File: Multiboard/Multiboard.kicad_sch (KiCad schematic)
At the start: 51 parts, among them J1 Conn_01x20_Socket, J2 Conn_01x20_Socket, J3 Debug, J4 USB_C_Receptacle_USB2.0_16P, SW1 BOOT0, SW2 NRST, SW8 KEY, U1 STM32F411RET6, U3 USART1, U4 I2C1, U5 SPI1, U6 ADC, U7 GPIO-PWM, U8 MCP1792x-3302xCB, Y1 32.768KHz, Y2 25MHz

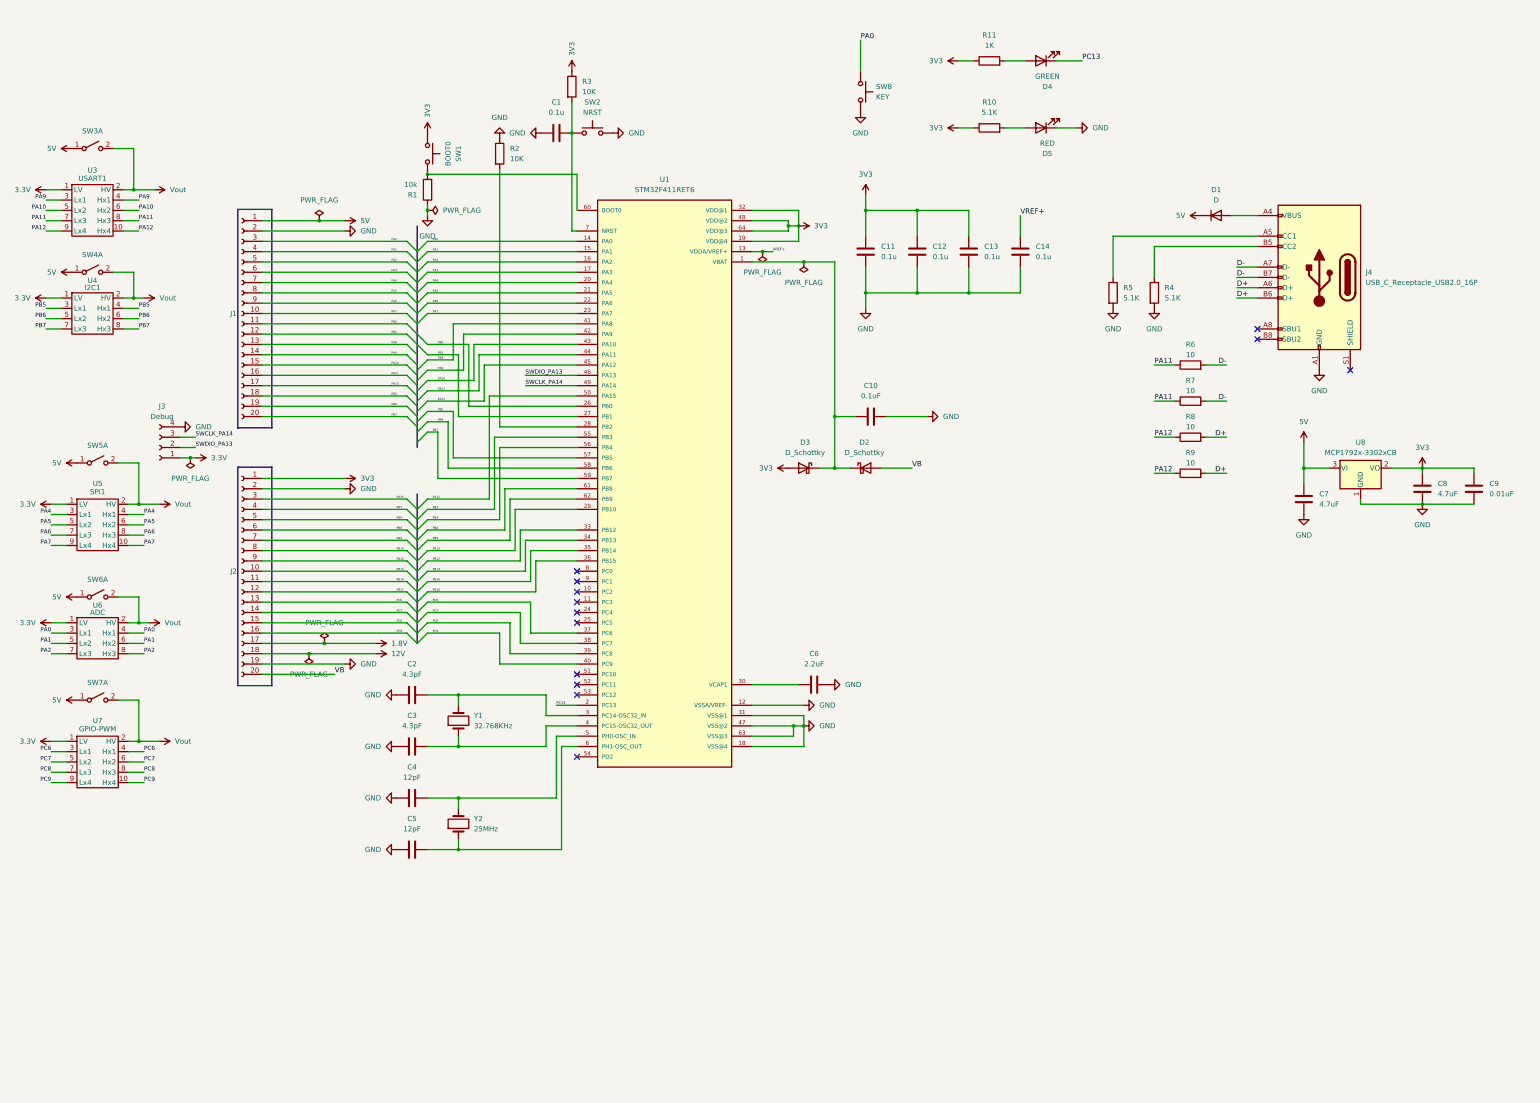
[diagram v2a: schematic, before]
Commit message: Fixed sch bus and added 12V charge pump
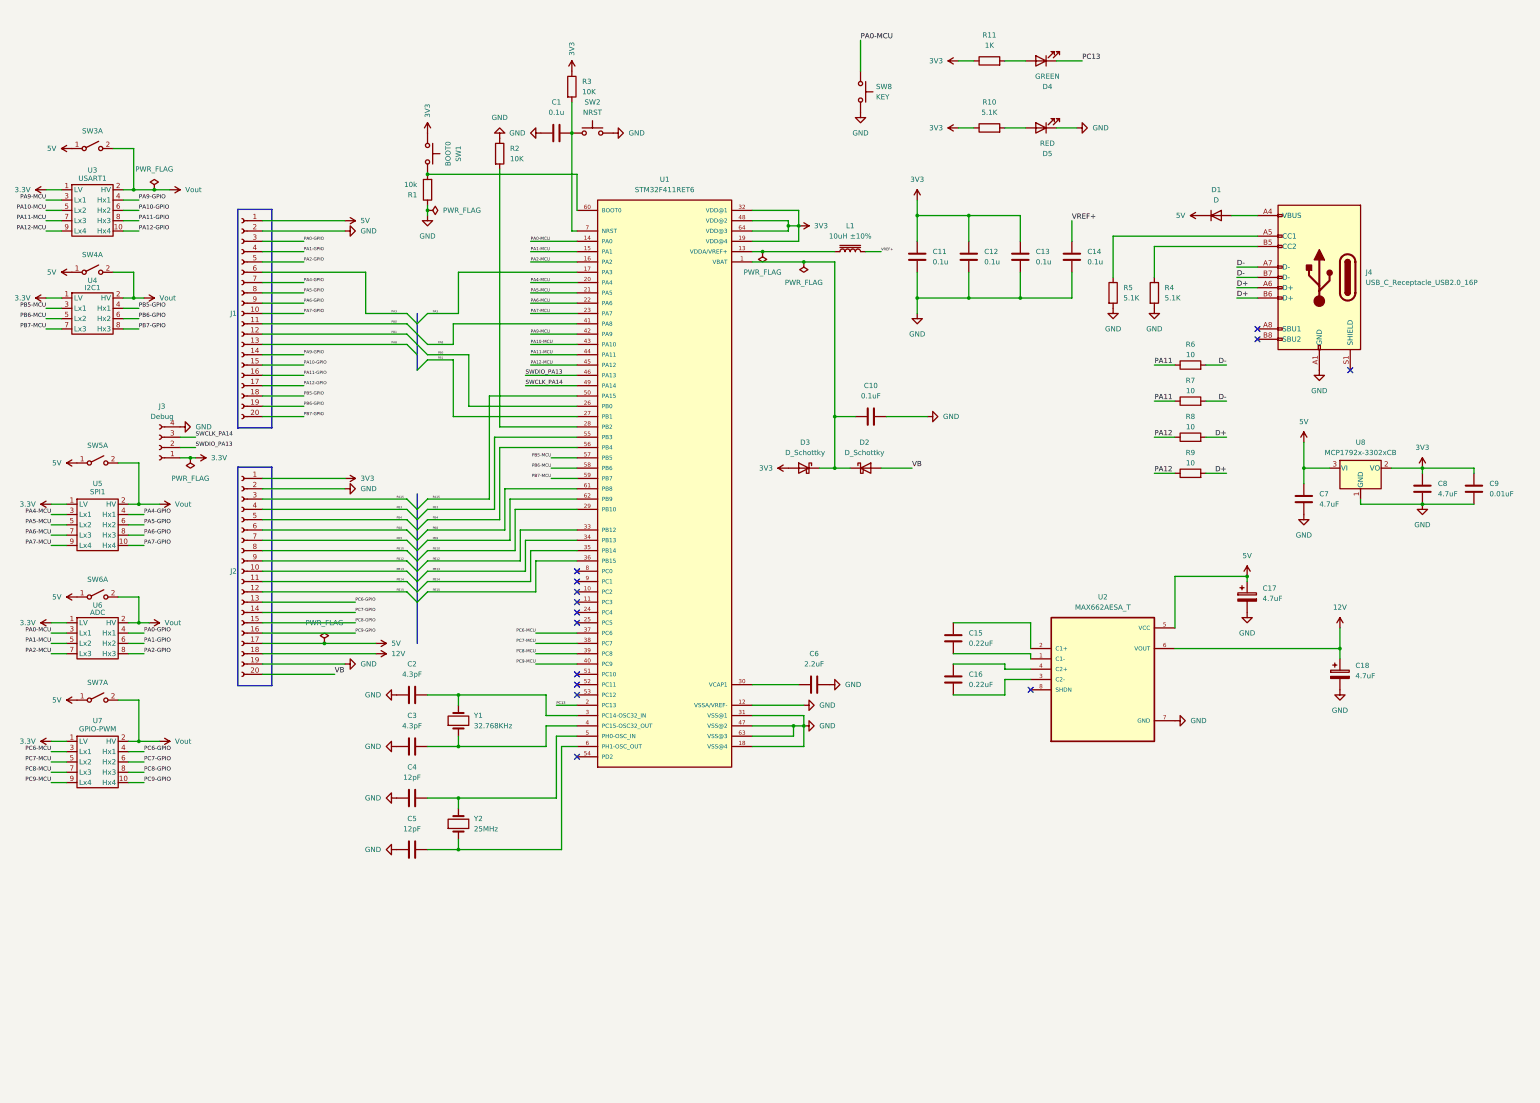
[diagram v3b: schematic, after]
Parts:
- added C15, C16: 0.22uF, symbol Device:C
- added C17, C18: 4.7uF, symbol Device:C_Polarized
- added L1: 10uH ±10%, Inductor_SMD:L_7.3x7.3_H4.5, symbol Device:L_Iron
- added U2: MAX662AESA_T, MAX662AESA_T:SOIC127P600X175-8N, symbol MAX662AESA_T:MAX662AESA_T
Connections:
- net 1.8V is gone; now on net 5V: J2.17 (Pin_17)
- net 12V: now also C18.1, U2.6 (VOUT)
- net 5V: now also C17.1, U2.5 (VCC)
- net GND: now also C17.2, C18.2, U2.7 (GND)
- net PA11: no longer J1.16 (Pin_16), U1.44 (PA11), U3.7 (Lx3), U3.8 (Hx3)
- net PA12: no longer J1.17 (Pin_17), U1.45 (PA12), U3.10 (Hx4), U3.9 (Lx4)
- net VREF+: now also L1.2; no longer U1.13 (VDDA/VREF+)
- net PA0 renamed PA0-MCU
- net PA0-MCU: no longer J1.3 (Pin_3), U6.4 (Hx1)
- net PA1 renamed PA1-GPIO
- net PA1-GPIO: no longer U1.15 (PA1), U6.5 (Lx2)
- net PA10 renamed PA10-GPIO
- net PA10-GPIO: no longer U1.43 (PA10), U3.5 (Lx2)
- net PA2 renamed PA2-GPIO
- net PA2-GPIO: no longer U1.16 (PA2), U6.7 (Lx3)
- net PA4 renamed PA4-GPIO
- net PA4-GPIO: no longer U1.20 (PA4), U5.3 (Lx1)
- net PA5 renamed PA5-GPIO
- net PA5-GPIO: no longer U1.21 (PA5), U5.5 (Lx2)
- net PA6 renamed PA6-GPIO
- net PA6-GPIO: no longer U1.22 (PA6), U5.7 (Lx3)
- net PA7 renamed PA7-GPIO
- net PA7-GPIO: no longer U1.23 (PA7), U5.9 (Lx4)
- net PA9 renamed PA9-GPIO
- net PA9-GPIO: no longer U1.42 (PA9), U3.3 (Lx1)
- net PB5 renamed PB5-GPIO
- net PB5-GPIO: no longer U1.57 (PB5), U4.3 (Lx1)
- net PB6 renamed PB6-GPIO
- net PB6-GPIO: no longer U1.58 (PB6), U4.5 (Lx2)
- net PB7 renamed PB7-GPIO
- net PB7-GPIO: no longer U1.59 (PB7), U4.7 (Lx3)
- net PC6 renamed PC6-GPIO
- net PC6-GPIO: no longer U1.37 (PC6), U7.3 (Lx1)
- net PC7 renamed PC7-GPIO
- net PC7-GPIO: no longer U1.38 (PC7), U7.5 (Lx2)
- net PC8 renamed PC8-GPIO
- net PC8-GPIO: no longer U1.39 (PC8), U7.7 (Lx3)
- net PC9 renamed PC9-GPIO
- net PC9-GPIO: no longer U1.40 (PC9), U7.9 (Lx4)
- new net: L1.1, U1.13 (VDDA/VREF+)
- new net: C15.1, U2.2 (C1+)
- new net: C15.2, U2.1 (C1-)
- new net: C16.1, U2.4 (C2+)
- new net: C16.2, U2.3 (C2-)
- new net PA0-GPIO: J1.3 (Pin_3), U6.4 (Hx1)
- new net PA1-MCU: U1.15 (PA1), U6.5 (Lx2)
- new net PA10-MCU: U1.43 (PA10), U3.5 (Lx2)
- new net PA11-GPIO: J1.16 (Pin_16), U3.8 (Hx3)
- new net PA11-MCU: U1.44 (PA11), U3.7 (Lx3)
- new net PA12-GPIO: J1.17 (Pin_17), U3.10 (Hx4)
- new net PA12-MCU: U1.45 (PA12), U3.9 (Lx4)
- new net PA2-MCU: U1.16 (PA2), U6.7 (Lx3)
- new net PA4-MCU: U1.20 (PA4), U5.3 (Lx1)
- new net PA5-MCU: U1.21 (PA5), U5.5 (Lx2)
- new net PA6-MCU: U1.22 (PA6), U5.7 (Lx3)
- new net PA7-MCU: U1.23 (PA7), U5.9 (Lx4)
- new net PA9-MCU: U1.42 (PA9), U3.3 (Lx1)
- new net PB5-MCU: U1.57 (PB5), U4.3 (Lx1)
- new net PB6-MCU: U1.58 (PB6), U4.5 (Lx2)
- new net PB7-MCU: U1.59 (PB7), U4.7 (Lx3)
- new net PC6-MCU: U1.37 (PC6), U7.3 (Lx1)
- new net PC7-MCU: U1.38 (PC7), U7.5 (Lx2)
- new net PC8-MCU: U1.39 (PC8), U7.7 (Lx3)
- new net PC9-MCU: U1.40 (PC9), U7.9 (Lx4)
- no-connect marks 13 -> 14
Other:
- moved on the sheet: C11, C12, C13, C14

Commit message: Put level shifters in nested schematic
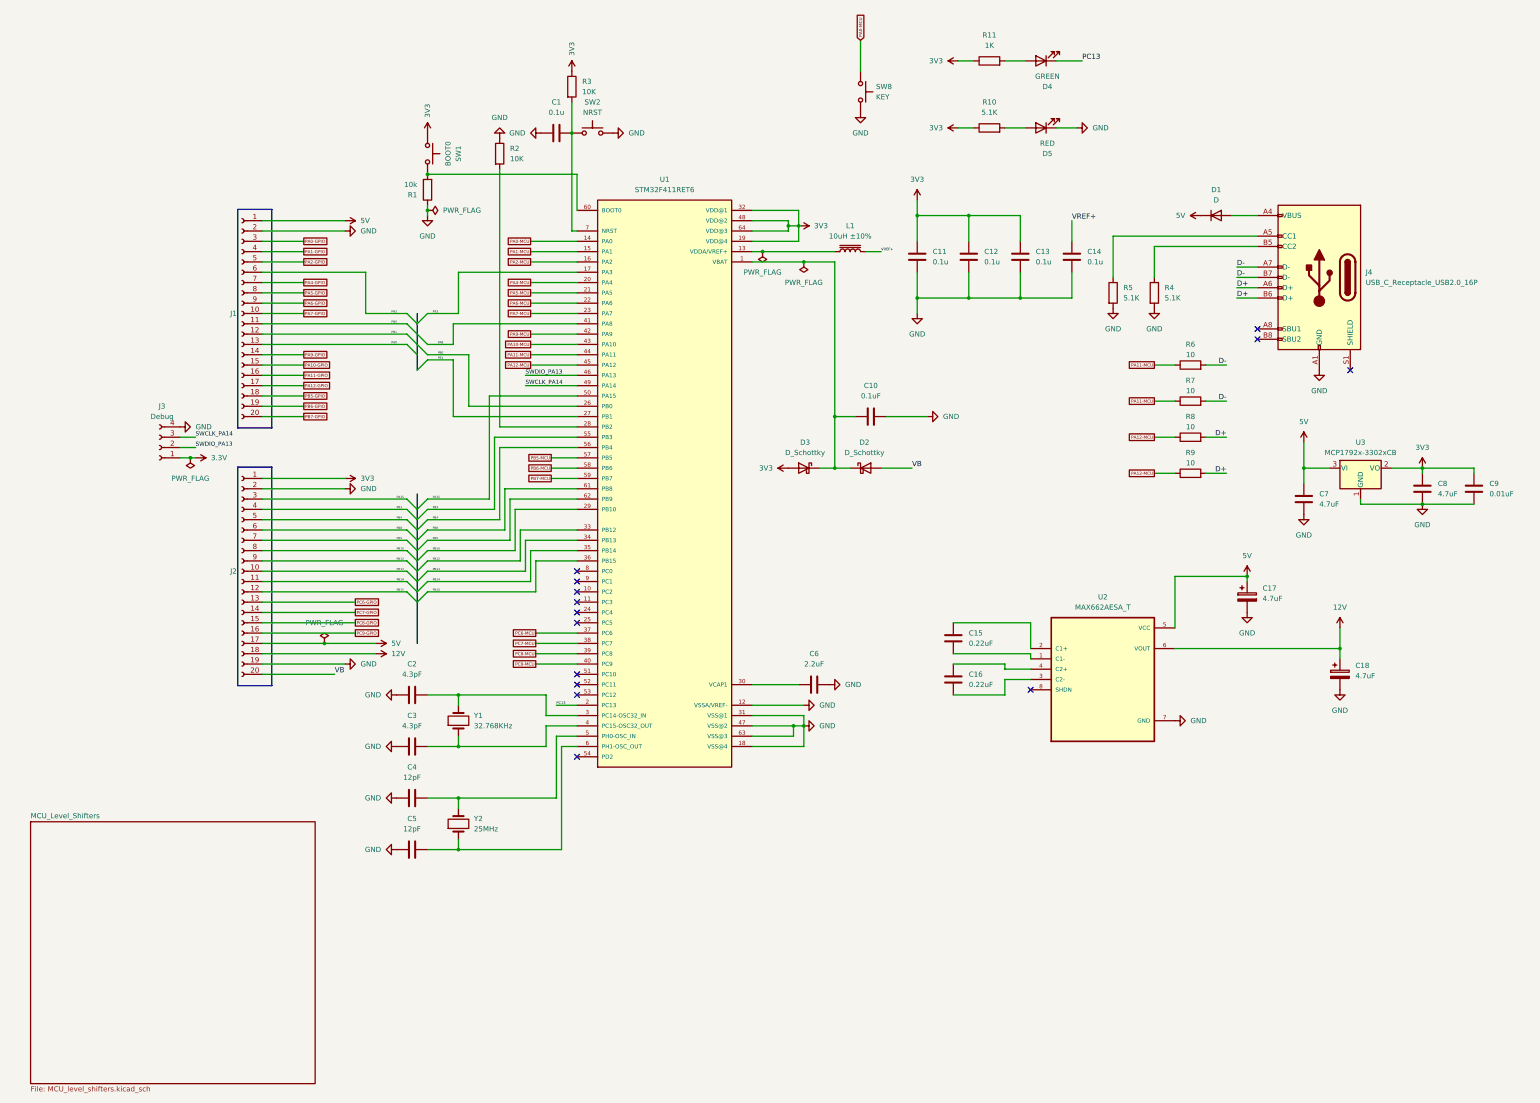
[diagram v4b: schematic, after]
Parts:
- removed SW3, SW4, SW5, SW6, SW7: ~, symbol Switch:SW_DPST_x2
- removed U3: USART1, symbol Level_Shifter:Level_Shifter_4_BD
- removed U4: I2C1, symbol Level_Shifter:Level_Shifter_3_BD
- removed U5: SPI1, symbol Level_Shifter:Level_Shifter_4_BD
- removed U6: ADC, symbol Level_Shifter:Level_Shifter_3_BD
- removed U7: GPIO-PWM, symbol Level_Shifter:Level_Shifter_4_BD
- C1, C10, C11, C12, C13, C14, C15, C16, C17, C18, C2, C3, C4, C5, C6, C7, C8, C9: footprint (none) -> Capacitor_SMD:C_0603_1608Metric_Pad1.08x0.95mm_HandSolder
- D1, D2, D3: footprint (none) -> Diode_SMD:D_0603_1608Metric_Pad1.05x0.95mm_HandSolder
- D4, D5: footprint (none) -> LED_SMD:LED_0603_1608Metric_Pad1.05x0.95mm_HandSolder
- J1, J2: footprint Connector_PinHeader_1.27mm:PinHeader_1x20_P1.27mm_Horizontal -> Connector_JST:JST_XA_B20B-XASK-1-A_1x20_P2.50mm_Vertical
- J3: footprint (none) -> Connector_Hirose:Hirose_DF13-04P-1.25DSA_1x04_P1.25mm_Vertical
- J4: footprint (none) -> Connector_USB:USB_C_Receptacle_G-Switch_GT-USB-7010ASV
- L1: footprint Inductor_SMD:L_7.3x7.3_H4.5 -> Inductor_SMD:L_0603_1608Metric_Pad1.05x0.95mm_HandSolder
- R1, R10, R11, R2, R3, R4, R5, R6, R7, R8, R9: footprint (none) -> Resistor_SMD:R_0603_1608Metric_Pad0.98x0.95mm_HandSolder
- SW1, SW2, SW8: footprint (none) -> Button_Switch_THT:SW_PUSH_6mm
- U2: footprint MAX662AESA_T:SOIC127P600X175-8N -> MAX662AESA+T:SOIC127P600X175-8N
- Y1, Y2: footprint (none) -> Crystal:Crystal_SMD_0603-2Pin_6.0x3.5mm_HandSoldering
- renumbered U8 to U3
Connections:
- net PA11 is gone; now on net PA11-MCU: R6.1, R7.1
- net PA12 is gone; now on net PA12-MCU: R8.1, R9.1
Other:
- added sheet MCU_Level_Shifters (MCU_level_shifters.kicad_sch)
